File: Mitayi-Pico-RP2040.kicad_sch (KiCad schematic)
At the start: 53 parts, among them J1 EXP8, J2 USB_C_Receptacle_USB2.0, J3 Header_1, J4 Header_2, J5 SWD, J6 USB_B_Micro, SW1 Reset, SW2 UBUT, U1 W25Q128JVS, U2 MIC5219-3.3YM5, U3 RP2040, Y1 YIC-12M20P2/XT324-10/10

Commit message: Updated to KiCad V8
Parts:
- D1: value PMEG4005EJ -> BS5817WS
- R10, R2: value 1k -> 1K
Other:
- note added: "3.3V Main"
- note added: "450mV @ 1A"
- note added: "Mounting Holes"
- note added: "USB-C"
- note removed: "Alt: B0540WS-7"
- note removed: "Main Regulator"
- note removed: "USB Type-C"
- company: CIRCUITSTATE Electronics LLP -> CIRCUITSTATE Electronics LLP (www.circuitstate.com)
- moved on the sheet: C1, C10, C11, C12, C13, C14, C15, C16, C17, C18, C19, C2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

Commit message: Updated fab layers
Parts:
- C1, C10, C11, C12, C2, C3, C6, C7, C8, C9: value 100n -> 0.1uF
- C13, C15: value 10u -> 10uF
- C19, C4, C5: value 1u -> 1uF
- D2: value DBG_LED -> Blue; Name (none) -> DBG_LED
- D3: value POW_LED -> Red; Name (none) -> POW_LED
- J1: Name (none) -> EXP8
- J2: value USB_C_Receptacle_USB2.0 -> USB-C-2.0; Name (none) -> USB-C
- J3: value Header_1 -> Header-1; Name (none) -> Header-1
- J4: value Header_2 -> Header-2; Name (none) -> Header-2
- J5: Name (none) -> SWD
- J6: Name (none) -> USB-Micro
- JP1: Name (none) -> AREF_SEL
- JP4: Name (none) -> VR1_CE
- JP5: Name (none) -> DEB_EN
- JP6: value UBUT_SEL -> BTN_SEL; Name (none) -> UBUT_SEL
- SW1: Name (none) -> Reset
- SW2: value UBUT -> BTN; Name (none) -> UBUT
- U3: Author CIRCUITSTATE Electronics -> (none); License CC BY 4.0 -> (none); Revision 1.3 -> (none)
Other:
- moved on the sheet: C3

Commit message: R0.6
* Added USB breakout pads.
* Moved BTN jumper to Front.
* Replaced jumpers with 0R.
* Udpated fab layers.
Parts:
- added J10: GND, CIRCUITSTATE_Pads:Solderpad_Rectangle_0.8x1.3mm_Chamfered, symbol Connector_Generic:Conn_01x01
- added J7: VBUS, CIRCUITSTATE_Pads:Solderpad_Rounded_Rectangle_0.8x1.3mm, symbol Connector_Generic:Conn_01x01
- added J8: DM, CIRCUITSTATE_Pads:Solderpad_Rounded_Rectangle_0.8x1.3mm, symbol Connector_Generic:Conn_01x01
- added J9: DP, CIRCUITSTATE_Pads:Solderpad_Rounded_Rectangle_0.8x1.3mm, symbol Connector_Generic:Conn_01x01
- C1, C10, C11, C12, C16, C17, C18, C19, C2, C3, C4, C5, C6, C7, C8, C9: footprint Capacitor_SMD:C_0402_1005Metric_Pad0.74x0.62mm_HandSolder -> Capacitor_SMD:C_0402_1005Metric
- D2: value Blue -> BLUE
- D3: value Red -> RED
- H1, H2, H3, H4, J1, J3, J4, J5, J6: MPN (none) -> DNP
- J2: footprint CIRCUITSTATE_Connector_USB:Korean-Hroparts-Elec_TYPE-C-31-M-12 -> Connector_USB:USB_C_Receptacle_HRO_TYPE-C-31-M-12
- JP1: value AREF_SEL -> 0R; footprint CIRCUITSTATE_Jumper_SMD:Solder-Jumper_2P_Open_0402 -> Resistor_SMD:R_0402_1005Metric_Pad0.72x0.64mm_HandSolder; MFR (none) -> Walsin; MPN (none) -> WR04X000PTL
- JP4: value VR1_CE -> 0R; footprint CIRCUITSTATE_Jumper_SMD:Solder-Jumper_2P_Open_0402 -> Resistor_SMD:R_0402_1005Metric_Pad0.72x0.64mm_HandSolder; MFR (none) -> Walsin; MPN (none) -> WR04X000PTL
- JP5: value DEB_EN -> 0R; footprint CIRCUITSTATE_Jumper_SMD:Solder-Jumper_2P_Open_0402 -> Resistor_SMD:R_0402_1005Metric_Pad0.72x0.64mm_HandSolder; MFR (none) -> Walsin; MPN (none) -> WR04X000PTL
- JP6: footprint CIRCUITSTATE_Jumper_SMD:Solder-Jumper_3P_Open_0402 -> CIRCUITSTATE_Jumper_SMD:SolderJumper-3_P0.83mm_Open_Rounded-Pad_0.85x1mm; Name UBUT_SEL -> BTN_SEL
- R1: footprint Resistor_SMD:R_0402_1005Metric_Pad0.72x0.64mm_HandSolder -> Resistor_SMD:R_0402_1005Metric; MPN (none) -> DNP
- R10, R11, R2, R3, R4, R5, R6, R7, R8, R9: footprint Resistor_SMD:R_0402_1005Metric_Pad0.72x0.64mm_HandSolder -> Resistor_SMD:R_0402_1005Metric
- SW1: value Reset -> UK-B0273-SP25Y; MFR (none) -> USAKRO; MPN (none) -> UK-B0273-SP25Y; Name Reset -> RESET
- SW2: value BTN -> UK-B0273-SP25Y; MFR (none) -> USAKRO; MPN (none) -> UK-B0273-SP25Y; Name UBUT -> BTN
- U1: value W25Q128JVS -> W25Q32JVSSIQ; MFR (none) -> Winbond; MPN (none) -> W25Q32JVSSIQ
- U2: MFR (none) -> Microchip; MPN (none) -> MIC5219-3.3YM5-TR
- U3: MFR (none) -> Raspberry Pi; MPN (none) -> RP2040-B2
- Y1: MFR (none) -> YIC; MPN (none) -> YIC-12M20P2/XT324-10/10
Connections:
- net GND: now also J10.1 (Pin_1)
- net USB_D+: now also J9.1 (Pin_1)
- net USB_D-: now also J8.1 (Pin_1)
- net VBUS: now also J7.1 (Pin_1)

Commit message: Generated mfr files
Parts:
- C1, C10, C11, C12, C2, C3, C6, C7, C8, C9: MFR (none) -> Walsin; MPN (none) -> 0402B104K160CT
- C13, C15: MFR (none) -> Walsin; MPN (none) -> 0603X106M6R3CT
- C14: MFR (none) -> KYOCERA AVX; MPN (none) -> TAJR225M016RNJ
- C16: MFR (none) -> Walsin; MPN (none) -> 0402N471J500LT
- C17, C18: MFR (none) -> Walsin; MPN (none) -> 0402N270J500LT
- C19, C4, C5: MFR (none) -> Walsin; MPN (none) -> 0402X105K160CT
- D1: MFR (none) -> Micro Commercial Co; MPN (none) -> B5817WS
- D2: MFR (none) -> Everlight; MPN (none) -> 19-213/BHC-ZL1M2RY/3T
- D3: MFR (none) -> Everlight; MPN (none) -> 19-21SURC/S530-A2/TR8
- J2: MFR (none) -> HCTL; MPN (none) -> HC-TYPE-C-16P-01A
- JP6: MPN (none) -> DNP
- R10, R2: MFR (none) -> Walsin; MPN (none) -> WR04X1001FTL
- R11, R3, R4: MFR (none) -> Walsin; MPN (none) -> WR04X5101FTL
- R5, R6: MFR (none) -> Walsin; MPN (none) -> WR04X27R0FTL
- R7, R8: MFR (none) -> Walsin; MPN (none) -> WR04X4700FTL
- R9: MFR (none) -> Walsin; MPN (none) -> WR04X1002FTL
- SW1, SW2: MPN UK-B0273-SP25Y -> UK-B0273-SP25Y

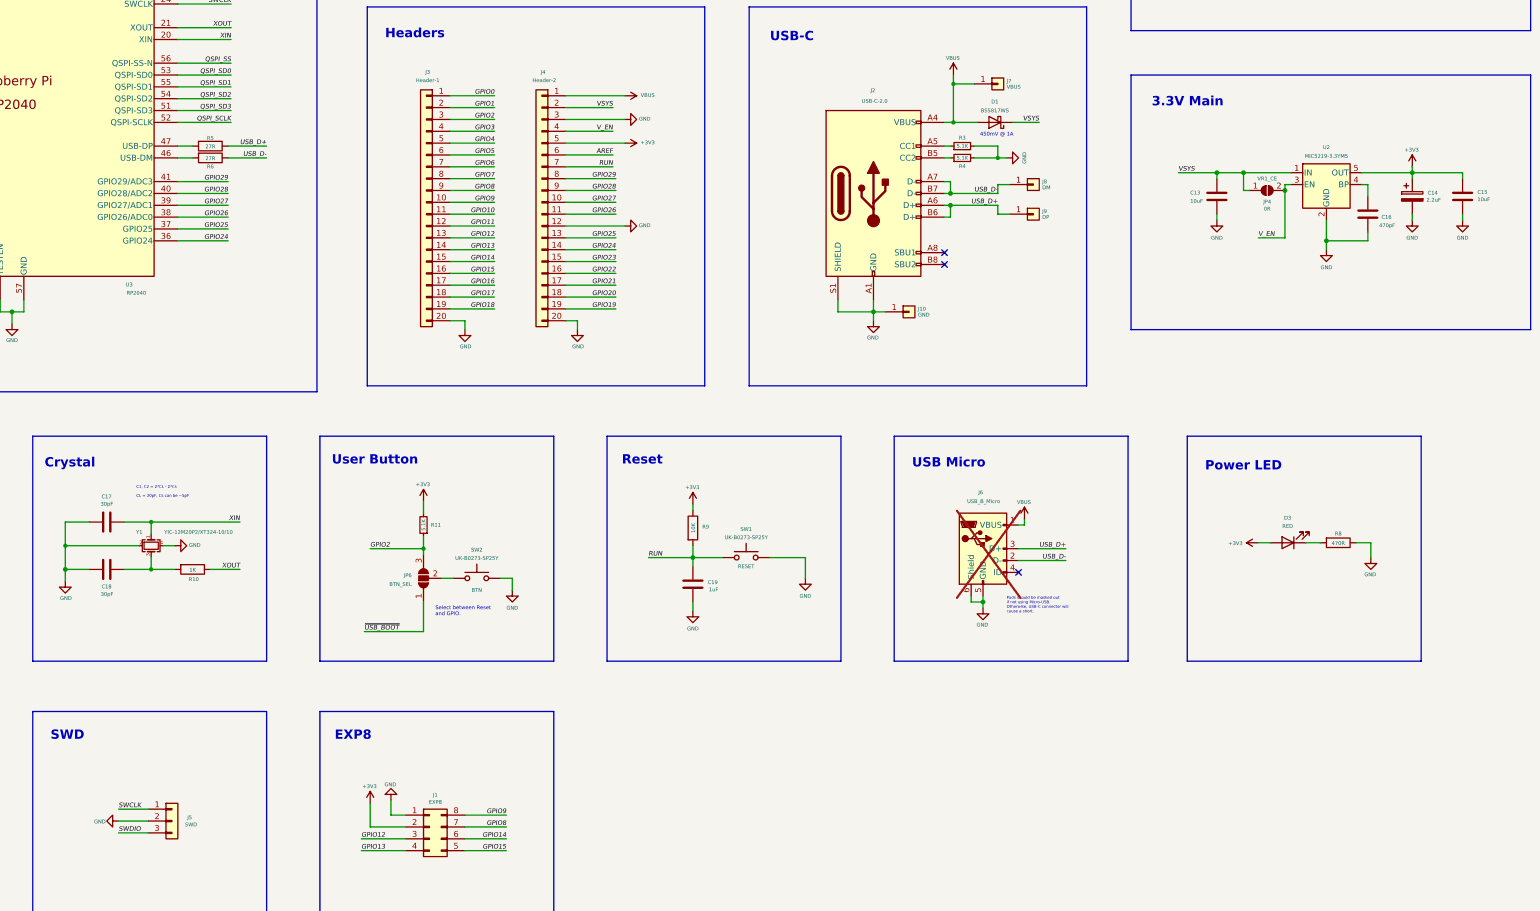
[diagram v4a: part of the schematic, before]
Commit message: Updated logos and labels
* Updated the silkscreen labels.
* Added the `D1` variant string to the project info and silkscreen.
* Added net classes and net highlights in the schematic and PCB.
* Updated the placements of the OSHW logo.
* Added `ALT MPN` column to the BoM.
* Manufacturing files generation pending.
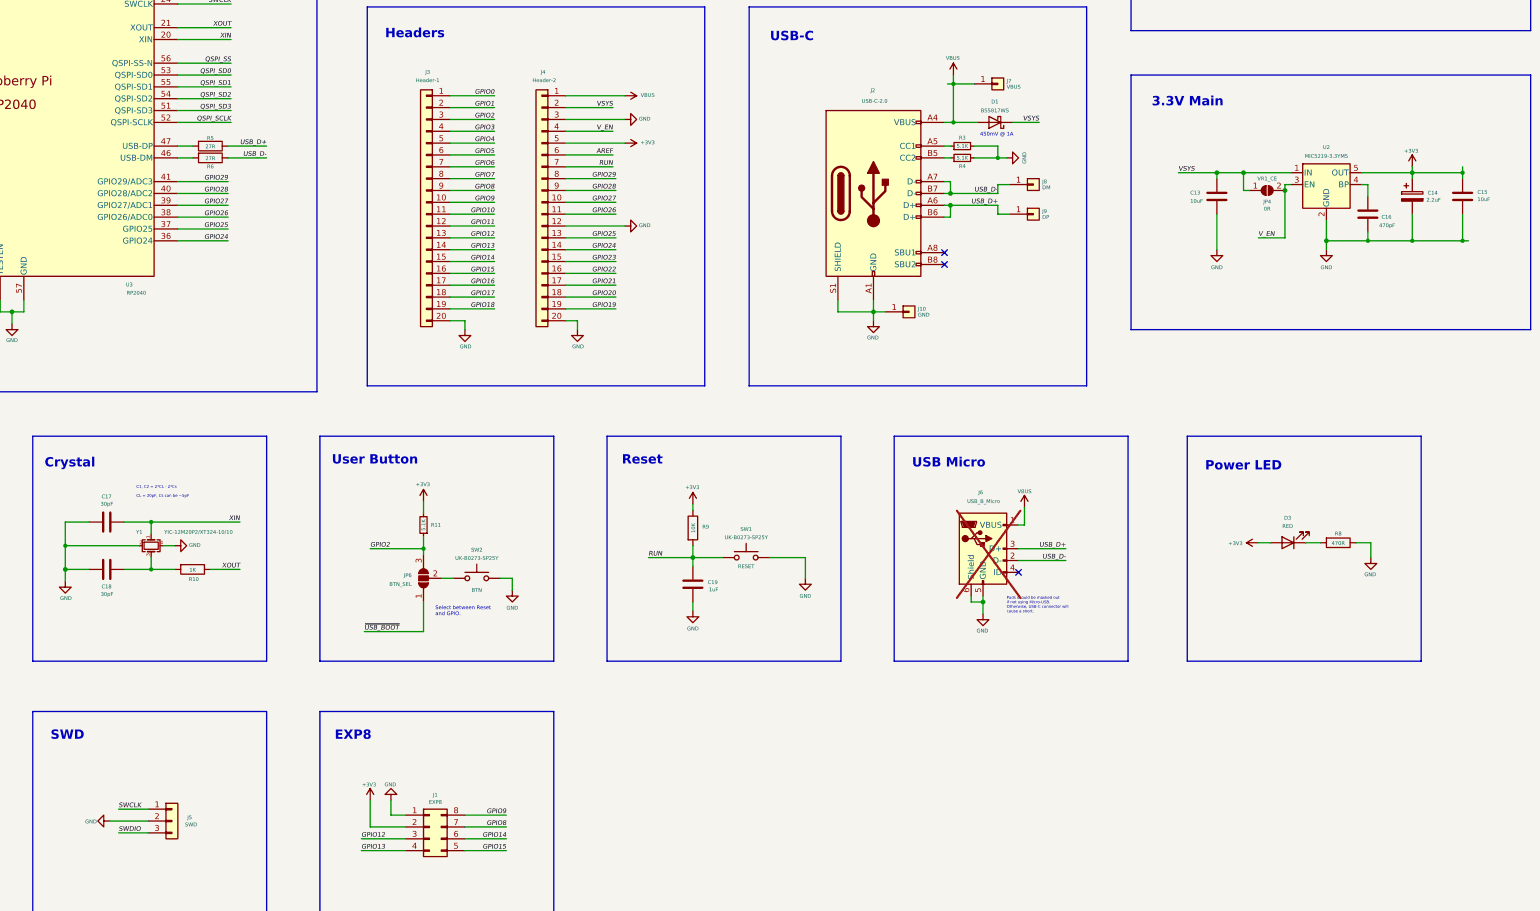
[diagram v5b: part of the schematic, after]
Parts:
- SW1, SW2: value UK-B0273-SP25Y -> UK-B0273-SP25Y
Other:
- title: Mitayi Pico - Schematic -> Mitayi Pico - D1

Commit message: Generated manufacturing files
- Replaced the USB-C connector with a custom one with paste layers on the THT pins. This will help in reliably soldering the USB-C connector.
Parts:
- J2: footprint Connector_USB:USB_C_Receptacle_HRO_TYPE-C-31-M-12 -> CIRCUITSTATE_Connector_USB:USB_C_Receptacle_HRO_TYPE-C-31-M-12
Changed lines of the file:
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@@
 			)
 		)
-		(property "Footprint" "Connector_USB:USB_C_Receptacle_HRO_TYPE-C-31-M-12"
+		(property "Footprint" "CIRCUITSTATE_Connector_USB:USB_C_Receptacle_HRO_TYPE-C-31-M-12"
 			(at 264.16 110.49 0)
 			(effects
@@
 			)
 		)
-		(property "ALT MPN" ""
+		(property "Alt MPN" ""
 			(at 260.35 110.49 0)
 			(effects
@@
 			)
 		)
-		(property "ALT MPN" ""
+		(property "Alt MPN" ""
 			(at 95.885 180.975 0)
 			(effects
@@
 			)
 		)
-		(property "ALT MPN" ""
+		(property "Alt MPN" ""
 			(at 192.405 41.91 0)
 			(effects
@@
 			)
 		)
-		(property "ALT MPN" ""
+		(property "Alt MPN" ""
 			(at 189.23 112.395 0)
 			(effects
@@
 			)
 		)
-		(property "ALT MPN" ""
+		(property "Alt MPN" ""
 			(at 286.385 95.25 0)
 			(effects
@@
 			)
 		)
-		(property "ALT MPN" ""
+		(property "Alt MPN" ""
 			(at 221.615 194.31 0)
 			(effects
@@
 			)
 		)
-		(property "ALT MPN" ""
+		(property "Alt MPN" ""
 			(at 368.935 52.07 0)
 			(effects
@@
 			)
 		)
-		(property "ALT MPN" ""
+		(property "Alt MPN" ""
 			(at 353.695 43.18 0)
 			(effects
@@
 			)
 		)
-		(property "ALT MPN" ""
+		(property "Alt MPN" ""
 			(at 227.33 41.91 0)
 			(effects
@@
 			)
 		)
-		(property "ALT MPN" ""
+		(property "Alt MPN" ""
 			(at 45.085 128.27 0)
 			(effects
@@
 			)
 		)
-		(property "ALT MPN" ""
+		(property "Alt MPN" ""
 			(at 165.1 246.38 0)
 			(effects
@@
 			)
 		)
-		(property "ALT MPN" ""
+		(property "Alt MPN" ""
 			(at 279.4 100.33 0)
 			(effects
@@
 			)
 		)
-		(property "ALT MPN" ""
+		(property "Alt MPN" ""
 			(at 375.285 38.1 0)
 			(effects
@@
 			)
 		)
-		(property "ALT MPN" ""
+		(property "Alt MPN" ""
 			(at 287.02 86.995 0)
 			(effects
@@
 			)
 		)
-		(property "ALT MPN" ""
+		(property "Alt MPN" ""
 			(at 294.64 108.585 0)
 			(effects
@@
 			)
 		)
-		(property "ALT MPN" ""
+		(property "Alt MPN" ""
 			(at 238.76 41.91 0)
 			(effects
@@
 			)
 		)
-		(property "ALT MPN" ""
+		(property "Alt MPN" ""
 			(at 221.615 182.245 0)
 			(effects
@@
 			)
 		)
-		(property "ALT MPN" ""
+		(property "Alt MPN" ""
 			(at 284.48 41.91 0)
 			(effects
@@
 			)
 		)
-		(property "ALT MPN" ""
+		(property "Alt MPN" ""
 			(at 279.4 102.87 0)
 			(effects
@@
 			)
 		)
-		(property "ALT MPN" ""
+		(property "Alt MPN" ""
 			(at 294.64 114.935 0)
 			(effects
@@
 			)
 		)
-		(property "ALT MPN" ""
+		(property "Alt MPN" ""
 			(at 36.195 245.745 0)
 			(effects
@@
 			)
 		)
-		(property "ALT MPN" ""
+		(property "Alt MPN" ""
 			(at 261.62 41.91 0)
 			(effects
@@
 			)
 		)
-		(property "ALT MPN" ""
+		(property "Alt MPN" ""
 			(at 215.9 41.91 0)
 			(effects
@@
 			)
 		)
-		(property "ALT MPN" ""
+		(property "Alt MPN" ""
 			(at 114.3 191.135 0)
 			(effects
@@
 			)
 		)
-		(property "ALT MPN" ""
+		(property "Alt MPN" ""
 			(at 38.354 189.23 0)
 			(effects
@@
 			)
 		)
-		(property "ALT MPN" ""
+		(property "Alt MPN" ""
 			(at 38.354 179.07 0)
 			(effects
@@
 			)
 		)
-		(property "ALT MPN" ""
+		(property "Alt MPN" ""
 			(at 172.085 41.91 0)
 			(effects
@@
 			)
 		)
-		(property "ALT MPN" ""
+		(property "Alt MPN" ""
 			(at 80.645 39.37 0)
 			(effects
@@
 			)
 		)
-		(property "ALT MPN" ""
+		(property "Alt MPN" ""
 			(at 164.465 112.395 0)
 			(effects
@@
 			)
 		)
-		(property "ALT MPN" ""
+		(property "Alt MPN" ""
 			(at 360.045 185.42 0)
 			(effects
@@
 			)
 		)
-		(property "ALT MPN" ""
+		(property "Alt MPN" ""
 			(at 182.245 41.91 0)
 			(effects
@@
 			)
 		)
-		(property "ALT MPN" ""
+		(property "Alt MPN" ""
 			(at 344.805 109.855 0)
 			(effects
@@
 			)
 		)
-		(property "ALT MPN" ""
+		(property "Alt MPN" ""
 			(at 375.92 111.125 0)
 			(effects
@@
 			)
 		)
-		(property "ALT MPN" ""
+		(property "Alt MPN" ""
 			(at 207.01 41.91 0)
 			(effects
@@
 			)
 		)
-		(property "ALT MPN" ""
+		(property "Alt MPN" ""
 			(at 273.05 41.91 0)
 			(effects
@@
 			)
 		)
-		(property "ALT MPN" ""
+		(property "Alt MPN" ""
 			(at 349.25 185.42 0)
 			(effects
@@
 			)
 		)
-		(property "ALT MPN" ""
+		(property "Alt MPN" ""
 			(at 334.01 111.125 0)
 			(effects
@@
 			)
 		)
-		(property "ALT MPN" ""
+		(property "Alt MPN" ""
 			(at 267.97 135.89 0)
 			(effects
@@
 			)
 		)
-		(property "ALT MPN" ""
+		(property "Alt MPN" ""
 			(at 250.19 41.91 0)
 			(effects
@@
 			)
 		)
-		(property "ALT MPN" ""
+		(property "Alt MPN" ""
 			(at 38.354 194.31 0)
 			(effects
@@
 			)
 		)
-		(property "ALT MPN" ""
+		(property "Alt MPN" ""
 			(at 45.72 245.745 0)
 			(effects
@@
 			)
 		)
-		(property "ALT MPN" ""
+		(property "Alt MPN" ""
 			(at 163.83 181.61 0)
 			(effects
@@
 			)
 		)
-		(property "ALT MPN" ""
+		(property "Alt MPN" ""
 			(at 118.11 100.33 0)
 			(effects
@@
 			)
 		)
-		(property "ALT MPN" ""
+		(property "Alt MPN" ""
 			(at 109.855 245.11 0)
 			(effects
@@
 			)
 		)
-		(property "ALT MPN" ""
+		(property "Alt MPN" ""
 			(at 366.395 114.935 0)
 			(effects
@@
 			)
 		)
-		(property "ALT MPN" ""
+		(property "Alt MPN" ""
 			(at 175.26 193.04 0)
 			(effects
@@
 			)
 		)
-		(property "ALT MPN" ""
+		(property "Alt MPN" ""
 			(at 118.11 102.87 0)
 			(effects
@@
 			)
 		)
-		(property "ALT MPN" ""
+		(property "Alt MPN" ""
 			(at 56.515 245.745 0)
 			(effects
@@
 			)
 		)
-		(property "ALT MPN" ""
+		(property "Alt MPN" ""
 			(at 38.354 184.15 0)
 			(effects
@@
 			)
 		)
-		(property "ALT MPN" ""
+		(property "Alt MPN" ""
 			(at 233.045 188.595 0)
 			(effects
@@
 			)
 		)
-		(property "ALT MPN" ""
+		(property "Alt MPN" ""
 			(at 163.83 193.04 0)
 			(effects
@@
 			)
 		)
-		(property "ALT MPN" ""
+		(property "Alt MPN" ""
 			(at 357.505 108.585 0)
 			(effects
@@
 			)
 		)
-		(property "ALT MPN" ""
+		(property "Alt MPN" ""
 			(at 338.455 49.53 0)
 			(effects
@@
 			)
 		)
-		(property "ALT MPN" ""
+		(property "Alt MPN" ""
 			(at 386.715 111.125 0)
 			(effects
@@
 			)
 		)
-		(property "ALT MPN" ""
+		(property "Alt MPN" ""
 			(at 105.41 186.055 0)
 			(effects
@@
 			)
 		)
-		(property "ALT MPN" ""
+		(property "Alt MPN" ""
 			(at 95.885 191.135 0)
 			(effects
@@
 			)
 		)
-		(property "ALT MPN" ""
+		(property "Alt MPN" ""
 			(at 283.845 186.69 0)
 			(effects
